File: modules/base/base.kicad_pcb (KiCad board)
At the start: 2 copper layers, 223.5 x 160 mm, 43 parts, among them J1 Ground, J2 Ground, J3 Ground, J4 Ground, J5 USB_C_Receptacle_PowerOnly_6P, U1 AMS1117-3.3

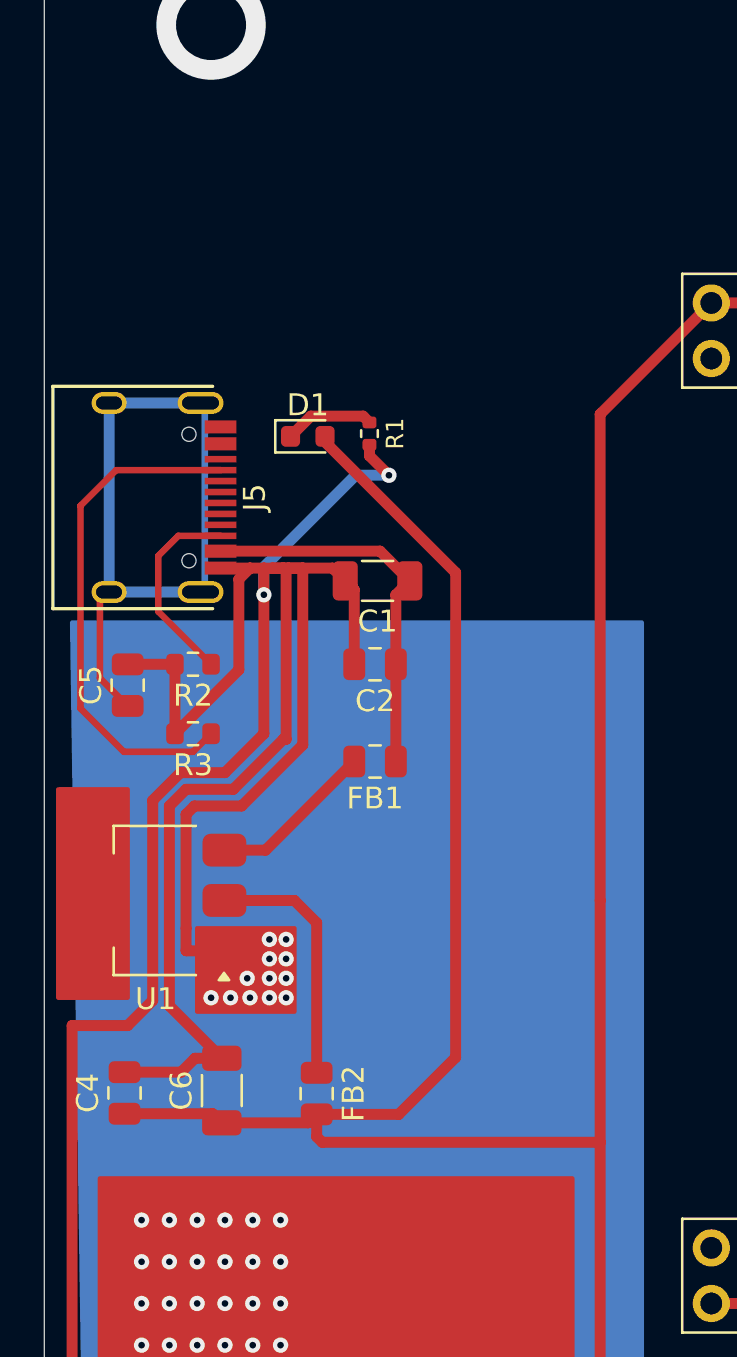
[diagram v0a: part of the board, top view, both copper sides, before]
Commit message: base: Add a reset button & use large caps
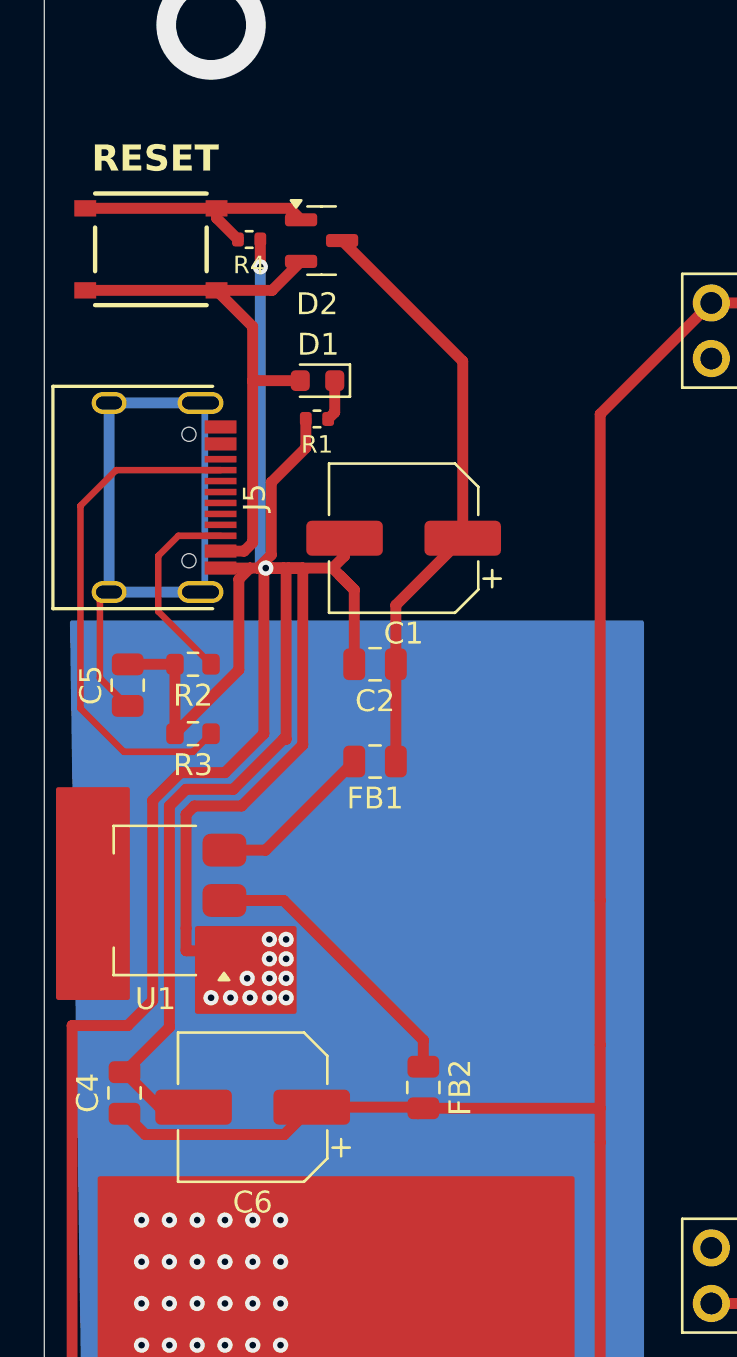
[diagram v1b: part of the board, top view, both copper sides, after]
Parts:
- added D2: SS8550, Package_TO_SOT_SMD:SOT-23, F.Cu at (43.1, 35.2)
- added R4: 10k, Resistor_SMD:R_0402_1005Metric, F.Cu at (39.8, 35.2)
- added SW1: SW_SPST, BreadModular_MISC:SPST_TS-1187A-B-A-B, F.Cu at (35.4, 35.6)
- C1, C6: value 100uf -> 470uf; footprint Capacitor_SMD:C_1206_3216Metric -> Capacitor_SMD:CP_Elec_6.3x7.7
- moved FB2 4.88 mm to (47.8, 74.0)
- moved D1 2.58 mm to (43.0, 41.6), turned to 180 degrees
- moved R1 2.49 mm to (42.9, 43.4), turned to 180 degrees
- moved C1 2.29 mm to (46.9, 48.9)
- moved C6 1.60 mm to (40.0, 74.8), turned to 180 degrees
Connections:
- C1 pad 1: +5V -> SWITCHED_5V
- C2 pad 1: +5V -> SWITCHED_5V
- D1 pad 2: +3.3V -> USB_5V
- FB1 pad 1: +5V -> SWITCHED_5V
- J5 pad A9: +5V -> USB_5V
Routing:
- net +3.3V: track 540.6 -> 502.1 mm
- net SWITCHED_5V: track 0.00 -> 27.4 mm
- net USB_5V: track 0.00 -> 26.4 mm
- net +5V: track 17.7 -> 0.00 mm
- net GND: track 1558.8 -> 1573.1 mm
- net Net-(SW1-A): track 0.00 -> 11.9 mm
- net Net-(D1-K): track 4.11 -> 1.87 mm
- net Net-(U1-VO): track 11.5 -> 12.9 mm
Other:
- board text added: "RESET"

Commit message: base_0.5.0
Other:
- board text added: "BASE 0.5.0"
- board text removed: "BASE 0.4.0"
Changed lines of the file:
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@@
 		)
 	)
-	(gr_text "BASE\n0.4.0"
+	(gr_text "BASE\n0.5.0"
 		(at 241.3 172.72 0)
 		(layer "F.SilkS")

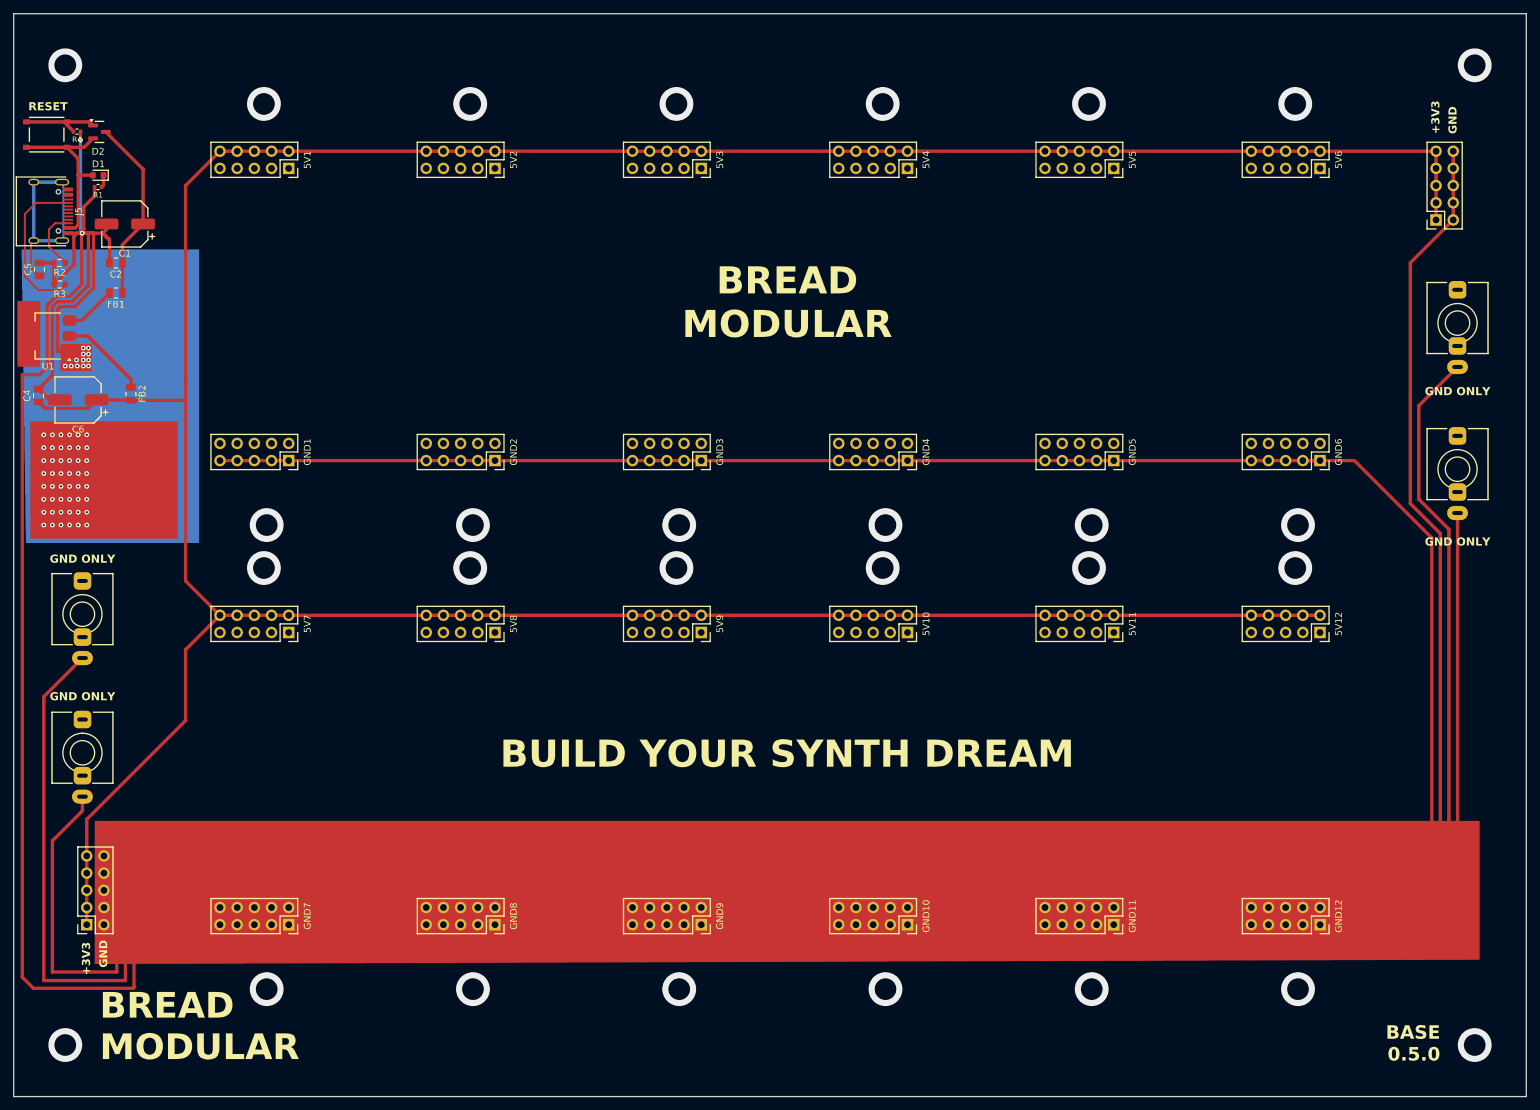
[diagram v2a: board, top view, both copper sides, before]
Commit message: Introduce headphone out into the base
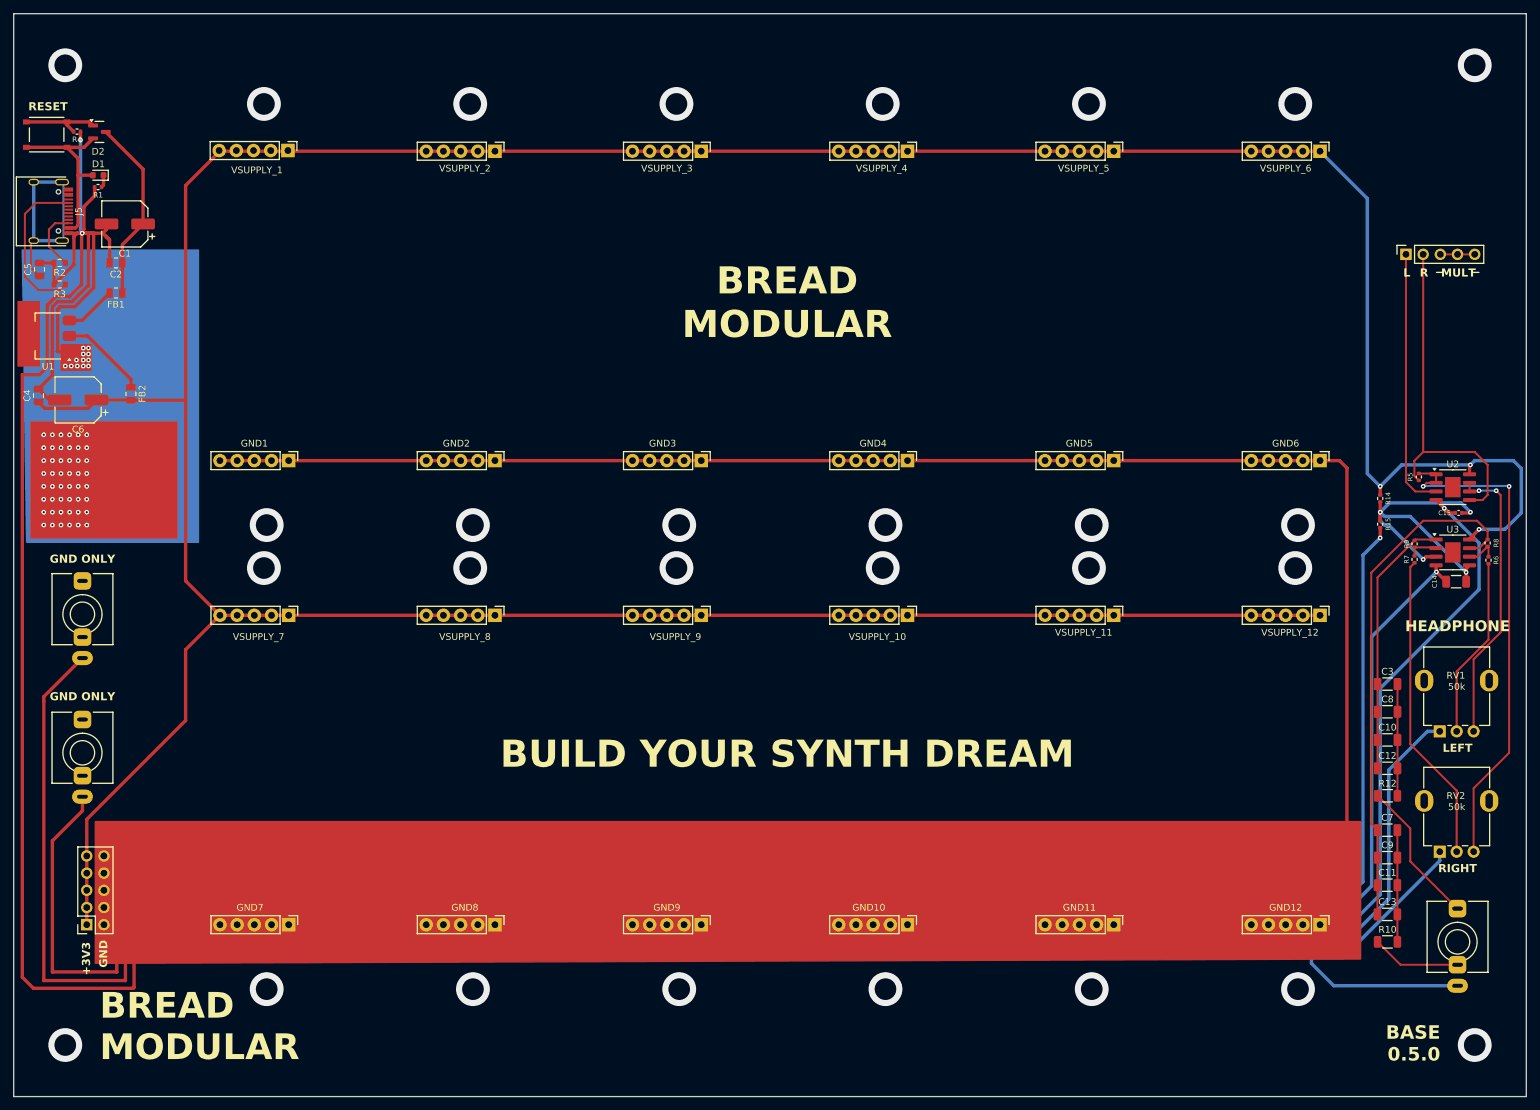
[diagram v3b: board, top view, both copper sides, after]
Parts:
- removed 5V13: Conn_02x05_Socket, Connector_PinSocket_2.54mm:PinSocket_2x05_P2.54mm_Vertical
- removed J1, J3: Ground, BreadModular_AudioJacks:Jack_3.5mm_QingPu_WQP-PJ366ST_Vertical
- added C10: 100uf, Capacitor_SMD:C_1206_3216Metric, F.Cu at (233.5, 125.1)
- added C11: 100uf, Capacitor_SMD:C_1206_3216Metric, F.Cu at (233.5, 146.6)
- added C12: 100uf, Capacitor_SMD:C_1206_3216Metric, F.Cu at (233.5, 129.3)
- added C13: 100uf, Capacitor_SMD:C_1206_3216Metric, F.Cu at (233.5, 150.9)
- added C14: 100uf, Capacitor_SMD:C_1206_3216Metric, F.Cu at (243.6, 101.7)
- added C15: 0.1uf, Capacitor_SMD:C_0402_1005Metric, F.Cu at (244.0, 91.6)
- added C3: 100uf, Capacitor_SMD:C_1206_3216Metric, F.Cu at (233.5, 116.8)
- added C7: 100uf, Capacitor_SMD:C_1206_3216Metric, F.Cu at (233.5, 138.4)
- added C8: 100uf, Capacitor_SMD:C_1206_3216Metric, F.Cu at (233.5, 120.9)
- added C9: 100uf, Capacitor_SMD:C_1206_3216Metric, F.Cu at (233.5, 142.5)
- added INPUT1: Conn_01x05_Socket, Connector_PinSocket_2.54mm:PinSocket_1x05_P2.54mm_Vertical, F.Cu at (236.2, 53.3)
- added J6: HeadphoneOut, BreadModular_AudioJacks:Jack_3.5mm_QingPu_WQP-PJ366ST_Vertical, F.Cu at (243.8, 154.9)
- added R10: 10, Resistor_SMD:R_1206_3216Metric, F.Cu at (233.5, 154.9)
- added R12: 10, Resistor_SMD:R_1206_3216Metric, F.Cu at (233.5, 133.3)
- added R14: 1k, Resistor_SMD:R_0402_1005Metric, F.Cu at (232.4, 89.4)
- added R15: 1k, Resistor_SMD:R_0402_1005Metric, F.Cu at (232.4, 93.2)
- added R5: 1M, Resistor_SMD:R_0402_1005Metric, F.Cu at (238.1, 86.2)
- added R6: 100k, Resistor_SMD:R_0402_1005Metric, F.Cu at (248.4, 98.5)
- added R7: 100k, Resistor_SMD:R_0402_1005Metric, F.Cu at (237.5, 98.4)
- added R8: 100k, Resistor_SMD:R_0402_1005Metric, F.Cu at (248.3, 96.0)
- added R9: 100k, Resistor_SMD:R_0402_1005Metric, F.Cu at (237.5, 96.1)
- added RV1: 50k, BreadModular_Pots:Potentiometer_RV09, F.Cu at (243.8, 116.8)
- added RV2: 50k, BreadModular_Pots:Potentiometer_RV09, F.Cu at (243.8, 134.6)
- added U2: MCP6002-xSN, Package_SO:SOIC-8-1EP_3.9x4.9mm_P1.27mm_EP2.29x3mm, F.Cu at (243.1, 87.7)
- added U3: MCP6002-xSN, Package_SO:SOIC-8-1EP_3.9x4.9mm_P1.27mm_EP2.29x3mm, F.Cu at (243.1, 97.4)
- GND1, GND10, GND11, GND12, GND2, GND3, GND4, GND5, GND6, GND7, GND8, GND9: footprint Connector_PinSocket_2.54mm:PinSocket_2x05_P2.54mm_Vertical -> BreadModular_MISC:Power_Connector
- VSUPPLY_1: renamed from 5V1; value Conn_02x05_Socket -> Conn_01x05_Socket; footprint Connector_PinSocket_2.54mm:PinSocket_2x05_P2.54mm_Vertical -> BreadModular_MISC:Power_Connector
- VSUPPLY_10: renamed from 5V10; footprint Connector_PinSocket_2.54mm:PinSocket_2x05_P2.54mm_Vertical -> BreadModular_MISC:Power_Connector
- VSUPPLY_11: renamed from 5V11; footprint Connector_PinSocket_2.54mm:PinSocket_2x05_P2.54mm_Vertical -> BreadModular_MISC:Power_Connector
- VSUPPLY_12: renamed from 5V12; footprint Connector_PinSocket_2.54mm:PinSocket_2x05_P2.54mm_Vertical -> BreadModular_MISC:Power_Connector
- VSUPPLY_2: renamed from 5V2; footprint Connector_PinSocket_2.54mm:PinSocket_2x05_P2.54mm_Vertical -> BreadModular_MISC:Power_Connector
- VSUPPLY_3: renamed from 5V3; footprint Connector_PinSocket_2.54mm:PinSocket_2x05_P2.54mm_Vertical -> BreadModular_MISC:Power_Connector
- VSUPPLY_4: renamed from 5V4; footprint Connector_PinSocket_2.54mm:PinSocket_2x05_P2.54mm_Vertical -> BreadModular_MISC:Power_Connector
- VSUPPLY_5: renamed from 5V5; footprint Connector_PinSocket_2.54mm:PinSocket_2x05_P2.54mm_Vertical -> BreadModular_MISC:Power_Connector
- VSUPPLY_6: renamed from 5V6; footprint Connector_PinSocket_2.54mm:PinSocket_2x05_P2.54mm_Vertical -> BreadModular_MISC:Power_Connector
- VSUPPLY_7: renamed from 5V7; footprint Connector_PinSocket_2.54mm:PinSocket_2x05_P2.54mm_Vertical -> BreadModular_MISC:Power_Connector
- VSUPPLY_8: renamed from 5V8; footprint Connector_PinSocket_2.54mm:PinSocket_2x05_P2.54mm_Vertical -> BreadModular_MISC:Power_Connector
- VSUPPLY_9: renamed from 5V9; footprint Connector_PinSocket_2.54mm:PinSocket_2x05_P2.54mm_Vertical -> BreadModular_MISC:Power_Connector
- moved VSUPPLY_1 2.64 mm to (71.0, 38.0)
- moved VSUPPLY_2 2.54 mm to (101.6, 38.1)
- moved VSUPPLY_3 2.54 mm to (132.1, 38.1)
- moved VSUPPLY_4 2.54 mm to (162.6, 38.1)
- moved VSUPPLY_5 2.54 mm to (193.0, 38.1)
- moved VSUPPLY_6 2.54 mm to (223.5, 38.1)
- moved VSUPPLY_10 2.54 mm to (162.6, 106.7)
- moved VSUPPLY_11 2.54 mm to (193.0, 106.7)
- moved VSUPPLY_12 2.54 mm to (223.5, 106.7)
- moved VSUPPLY_7 2.54 mm to (71.1, 106.7)
- moved VSUPPLY_8 2.54 mm to (101.6, 106.7)
- moved VSUPPLY_9 2.54 mm to (132.1, 106.7)
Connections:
- GND1 pad 2: unconnected-(GND1-Pin_2-Pad2) -> GND
- GND1 pad 4: unconnected-(GND1-Pin_4-Pad4) -> GND
- GND2 pad 2: unconnected-(GND2-Pin_2-Pad2) -> GND
- GND2 pad 4: unconnected-(GND2-Pin_4-Pad4) -> GND
- GND3 pad 2: unconnected-(GND3-Pin_2-Pad2) -> GND
- GND3 pad 4: unconnected-(GND3-Pin_4-Pad4) -> GND
- GND4 pad 2: unconnected-(GND4-Pin_2-Pad2) -> GND
- GND4 pad 4: unconnected-(GND4-Pin_4-Pad4) -> GND
- GND5 pad 2: unconnected-(GND5-Pin_2-Pad2) -> GND
- GND5 pad 4: unconnected-(GND5-Pin_4-Pad4) -> GND
- GND6 pad 2: unconnected-(GND6-Pin_2-Pad2) -> GND
- GND6 pad 4: unconnected-(GND6-Pin_4-Pad4) -> GND
- VSUPPLY_1 pad 1: unconnected-(5V1-Pin_1-Pad1) -> +3.3V
- VSUPPLY_1 pad 3: unconnected-(5V1-Pin_3-Pad3) -> +3.3V
- VSUPPLY_1 pad 5: unconnected-(5V1-Pin_5-Pad5) -> +3.3V
- VSUPPLY_10 pad 1: unconnected-(5V10-Pin_1-Pad1) -> +3.3V
- VSUPPLY_10 pad 3: unconnected-(5V10-Pin_3-Pad3) -> +3.3V
- VSUPPLY_10 pad 5: unconnected-(5V10-Pin_5-Pad5) -> +3.3V
- VSUPPLY_11 pad 1: unconnected-(5V11-Pin_1-Pad1) -> +3.3V
- VSUPPLY_11 pad 3: unconnected-(5V11-Pin_3-Pad3) -> +3.3V
- VSUPPLY_11 pad 5: unconnected-(5V11-Pin_5-Pad5) -> +3.3V
- VSUPPLY_12 pad 1: unconnected-(5V12-Pin_1-Pad1) -> +3.3V
- VSUPPLY_12 pad 3: unconnected-(5V12-Pin_3-Pad3) -> +3.3V
- VSUPPLY_12 pad 5: unconnected-(5V12-Pin_5-Pad5) -> +3.3V
- VSUPPLY_2 pad 1: unconnected-(5V2-Pin_1-Pad1) -> +3.3V
- VSUPPLY_2 pad 3: unconnected-(5V2-Pin_3-Pad3) -> +3.3V
- VSUPPLY_2 pad 5: unconnected-(5V2-Pin_5-Pad5) -> +3.3V
- VSUPPLY_3 pad 1: unconnected-(5V3-Pin_1-Pad1) -> +3.3V
- VSUPPLY_3 pad 3: unconnected-(5V3-Pin_3-Pad3) -> +3.3V
- VSUPPLY_3 pad 5: unconnected-(5V3-Pin_5-Pad5) -> +3.3V
- VSUPPLY_4 pad 1: unconnected-(5V4-Pin_1-Pad1) -> +3.3V
- VSUPPLY_4 pad 3: unconnected-(5V4-Pin_3-Pad3) -> +3.3V
- VSUPPLY_4 pad 5: unconnected-(5V4-Pin_5-Pad5) -> +3.3V
- VSUPPLY_5 pad 1: unconnected-(5V5-Pin_1-Pad1) -> +3.3V
- VSUPPLY_5 pad 3: unconnected-(5V5-Pin_3-Pad3) -> +3.3V
- VSUPPLY_5 pad 5: unconnected-(5V5-Pin_5-Pad5) -> +3.3V
- VSUPPLY_6 pad 1: unconnected-(5V6-Pin_1-Pad1) -> +3.3V
- VSUPPLY_6 pad 3: unconnected-(5V6-Pin_3-Pad3) -> +3.3V
- VSUPPLY_6 pad 5: unconnected-(5V6-Pin_5-Pad5) -> +3.3V
- VSUPPLY_7 pad 1: unconnected-(5V7-Pin_1-Pad1) -> +3.3V
- VSUPPLY_7 pad 3: unconnected-(5V7-Pin_3-Pad3) -> +3.3V
- VSUPPLY_7 pad 5: unconnected-(5V7-Pin_5-Pad5) -> +3.3V
- VSUPPLY_8 pad 1: unconnected-(5V8-Pin_1-Pad1) -> +3.3V
- VSUPPLY_8 pad 3: unconnected-(5V8-Pin_3-Pad3) -> +3.3V
- VSUPPLY_8 pad 5: unconnected-(5V8-Pin_5-Pad5) -> +3.3V
- VSUPPLY_9 pad 1: unconnected-(5V9-Pin_1-Pad1) -> +3.3V
- VSUPPLY_9 pad 3: unconnected-(5V9-Pin_3-Pad3) -> +3.3V
- VSUPPLY_9 pad 5: unconnected-(5V9-Pin_5-Pad5) -> +3.3V
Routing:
- net GND: track 1573.1 -> 1103.9 mm, vias 62 -> 65
- net Net-(C11-Pad1): track 0.00 -> 76.3 mm
- net Net-(U2A--): track 0.00 -> 74.9 mm, vias 0 -> 2
- net +3.3V: track 502.1 -> 569.5 mm, vias 0 -> 3
- net IN_R: track 0.00 -> 52.0 mm
- net +2.5V: track 0.00 -> 49.7 mm, vias 0 -> 4
- net Net-(R7-Pad1): track 0.00 -> 45.8 mm
- net Net-(U2B--): track 0.00 -> 42.8 mm, vias 0 -> 2
- net Net-(C10-Pad1): track 0.00 -> 39.2 mm
- net IN_L: track 0.00 -> 38.7 mm
- net Net-(R6-Pad1): track 0.00 -> 26.7 mm
- net OUT_L: track 0.00 -> 21.6 mm
- net Net-(C11-Pad2): track 0.00 -> 16.5 mm
- net Net-(C10-Pad2): track 0.00 -> 16.5 mm
- net OUT_R: track 0.00 -> 13.2 mm
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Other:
- board text added: "HEADPHONE"
- board text added: "L"
- board text added: "LEFT"
- board text added: "MULT"
- board text added: "R"
- board text added: "RIGHT"
